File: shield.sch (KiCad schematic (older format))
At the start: 22 parts, among them J1 E5V_Conn, P1 CONN_01X03, P2 CONN_02X10, P3 CONN_01X05, P4 CONN_01X05, P5 CONN_01X05, P6 5V_CAN_SELECT, P7 CONN_02X05, Q1 Q_PMOS_DGS, U1 ST_Nucleo144_F429ZI_Morpho

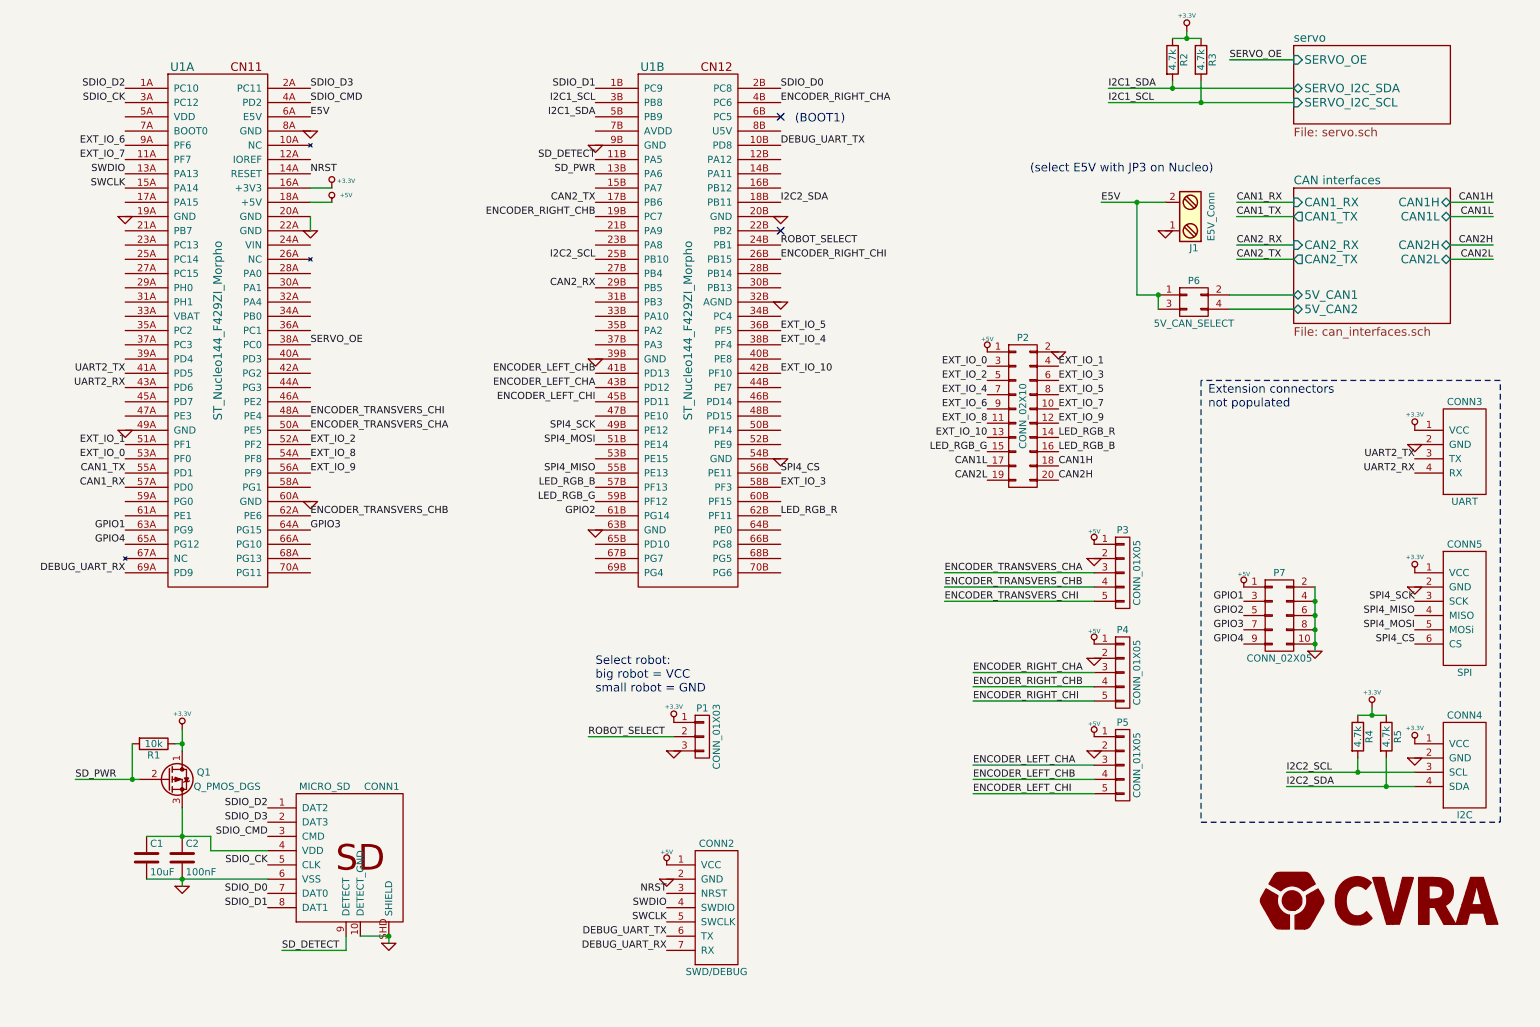
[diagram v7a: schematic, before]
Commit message: place parts in PCB
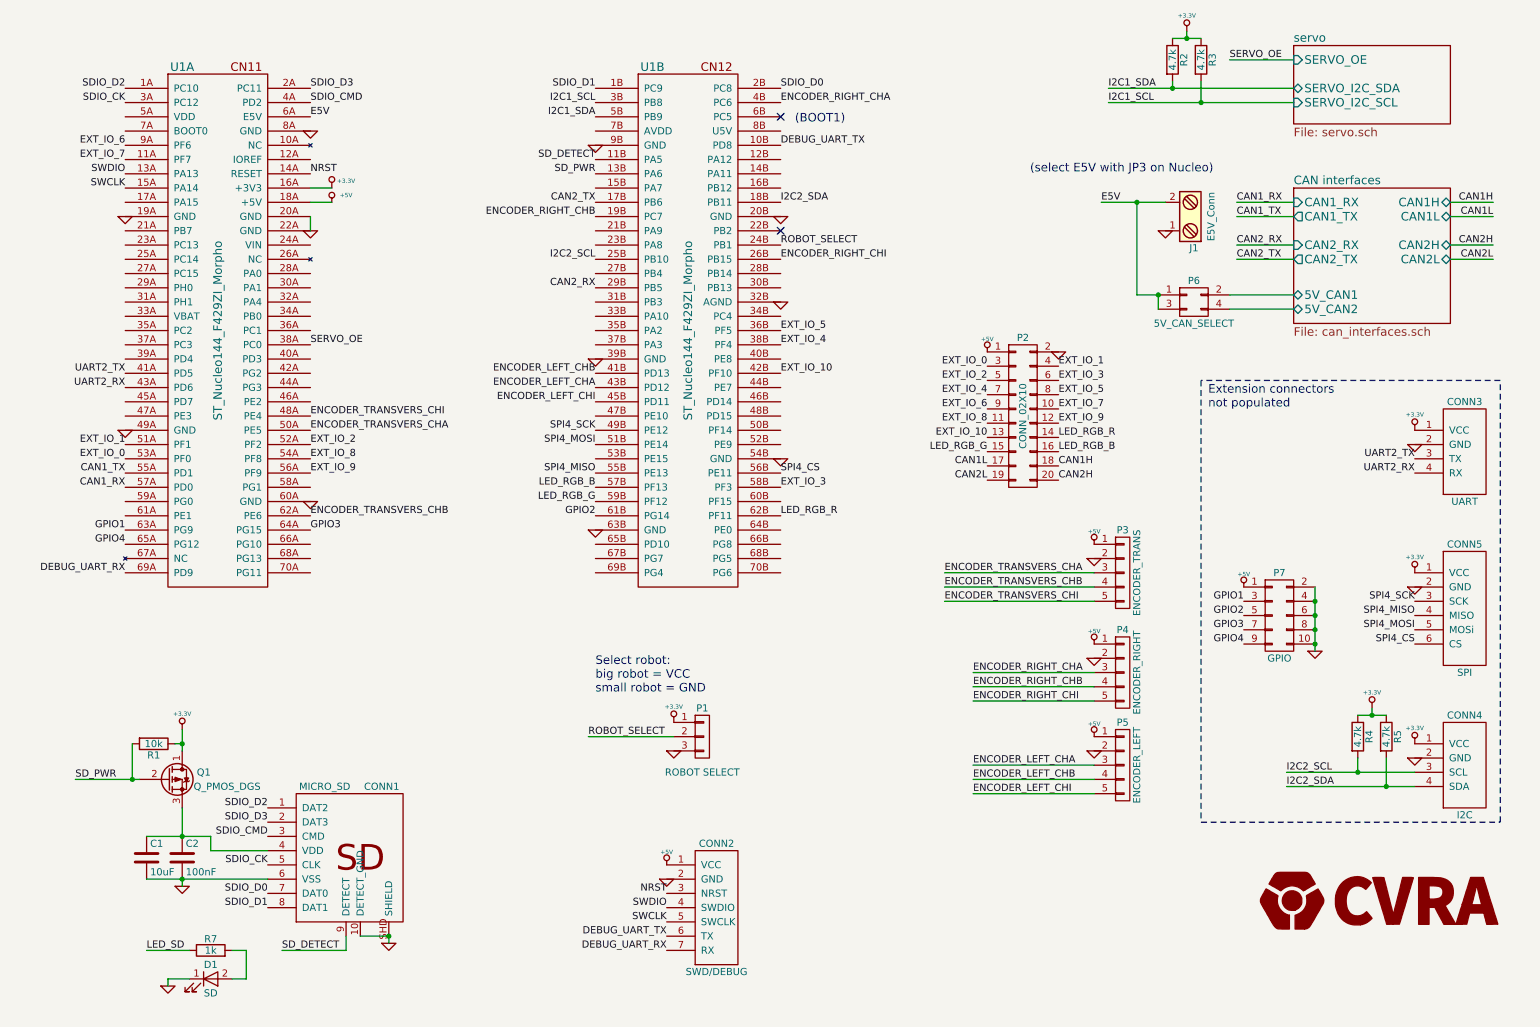
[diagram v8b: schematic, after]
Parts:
- added D1: SD, LEDs:LED_0805, symbol LED
- added R7: 1k, Resistors_SMD:R_0805, symbol R
- C2: footprint Capacitors_SMD:C_0603 -> Capacitors_SMD:C_0805
- CONN2: footprint _connectors:_Molex-PicoBlade-SMD-7 -> Connectors_Molex:Molex_PicoBlade_53047-0710_07x1.25mm_Straight
- P1: value CONN_01X03 -> ROBOT SELECT
- P2: footprint Pin_Headers:Pin_Header_Straight_2x10 -> Connect:IDC_Header_Straight_20pins
- P3: value CONN_01X05 -> ENCODER_TRANS
- P4: value CONN_01X05 -> ENCODER_RIGHT
- P5: value CONN_01X05 -> ENCODER_LEFT
- P7: value CONN_02X05 -> GPIO; footprint Pin_Headers:Pin_Header_Straight_2x05 -> Connect:IDC_Header_Straight_10pins
- R1, R2, R3, R4, R5: footprint Resistors_SMD:R_0603 -> Resistors_SMD:R_0805
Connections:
- net GND: now also D1.1 (K)
- new net: D1.2 (A), R7.2
- new net LED_SD: R7.1
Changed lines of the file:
@@
 F 0 "C2" H 1825 6650 50  0000 L CNN
 F 1 "100nF" H 1825 6450 50  0000 L CNN
-F 2 "Capacitors_SMD:C_0603" H 1838 6400 50  0001 C CNN
+F 2 "Capacitors_SMD:C_0805" H 1838 6400 50  0001 C CNN
 F 3 "" H 1800 6550 50  0000 C CNN
 	1    1800 6550
@@
 F 0 "R1" V 1680 5750 50  0000 C CNN
 F 1 "10k" V 1600 5750 50  0000 C CNN
-F 2 "Resistors_SMD:R_0603" V 1530 5750 50  0001 C CNN
+F 2 "Resistors_SMD:R_0805" V 1530 5750 50  0001 C CNN
 F 3 "" H 1600 5750 50  0000 C CNN
 	1    1600 5750
@@
 F 0 "P2" H 7700 4000 50  0000 C CNN
 F 1 "CONN_02X10" V 7700 3450 50  0000 C CNN
-F 2 "Pin_Headers:Pin_Header_Straight_2x10" H 7700 2250 50  0001 C CNN
+F 2 "Connect:IDC_Header_Straight_20pins" H 7700 2250 50  0001 C CNN
 F 3 "" H 7700 2250 50  0000 C CNN
 	1    7700 3450
@@
 P 9500 4850
 F 0 "P7" H 9500 5150 50  0000 C CNN
-F 1 "CONN_02X05" H 9500 4550 50  0000 C CNN
-F 2 "Pin_Headers:Pin_Header_Straight_2x05" H 9500 3650 50  0001 C CNN
+F 1 "GPIO" H 9500 4550 50  0000 C CNN
+F 2 "Connect:IDC_Header_Straight_10pins" H 9500 3650 50  0001 C CNN
 F 3 "" H 9500 3650 50  0000 C CNN
 	1    9500 4850
@@
 P 8400 5250
 F 0 "P4" H 8400 5550 50  0000 C CNN
-F 1 "CONN_01X05" V 8500 5250 50  0000 C CNN
+F 1 "ENCODER_RIGHT" V 8500 5250 50  0000 C CNN
 F 2 "_connectors:Molex-PicoBlade-5" H 8400 5250 50  0001 C CNN
 F 3 "" H 8400 5250 50  0000 C CNN
@@
 P 8400 5900
 F 0 "P5" H 8400 6200 50  0000 C CNN
-F 1 "CONN_01X05" V 8500 5900 50  0000 C CNN
+F 1 "ENCODER_LEFT" V 8500 5900 50  0000 C CNN
 F 2 "_connectors:Molex-PicoBlade-5" H 8400 5900 50  0001 C CNN
 F 3 "" H 8400 5900 50  0000 C CNN
@@
 P 8400 4550
 F 0 "P3" H 8400 4850 50  0000 C CNN
-F 1 "CONN_01X05" V 8500 4550 50  0000 C CNN
+F 1 "ENCODER_TRANS" V 8500 4550 50  0000 C CNN
 F 2 "_connectors:Molex-PicoBlade-5" H 8400 4550 50  0001 C CNN
 F 3 "" H 8400 4550 50  0000 C CNN
@@
 F 0 "CONN2" H 5550 7350 50  0000 C CNN
 F 1 "SWD/DEBUG" H 5550 6450 50  0000 C CNN
-F 2 "_connectors:_Molex-PicoBlade-SMD-7" H 5550 6850 50  0001 C CNN
+F 2 "Connectors_Molex:Molex_PicoBlade_53047-0710_07x1.25mm_Straight" H 5550 6850 50  0001 C CNN
 F 3 "DOCUMENTATION" H 5550 6850 50  0001 C CNN
 	1    5550 6900
@@
 P 5450 5700
 F 0 "P1" H 5450 5900 50  0000 C CNN
-F 1 "CONN_01X03" V 5550 5700 50  0000 C CNN
+F 1 "ROBOT SELECT" H 5450 5450 50  0000 C CNN
 F 2 "Pin_Headers:Pin_Header_Straight_1x03" H 5450 5700 50  0001 C CNN
 F 3 "" H 5450 5700 50  0000 C CNN
@@
 F 0 "R4" V 10130 5700 50  0000 C CNN
 F 1 "4.7k" V 10050 5700 50  0000 C CNN
-F 2 "Resistors_SMD:R_0603" V 9980 5700 50  0001 C CNN
+F 2 "Resistors_SMD:R_0805" V 9980 5700 50  0001 C CNN
 F 3 "" H 10050 5700 50  0000 C CNN
 	1    10050 5700
@@
 F 0 "R5" V 10330 5700 50  0000 C CNN
 F 1 "4.7k" V 10250 5700 50  0000 C CNN
-F 2 "Resistors_SMD:R_0603" V 10180 5700 50  0001 C CNN
+F 2 "Resistors_SMD:R_0805" V 10180 5700 50  0001 C CNN
 F 3 "" H 10250 5700 50  0000 C CNN
 	1    10250 5700
@@
 F 0 "R2" V 8830 950 50  0000 C CNN
 F 1 "4.7k" V 8750 950 50  0000 C CNN
-F 2 "Resistors_SMD:R_0603" V 8680 950 50  0001 C CNN
+F 2 "Resistors_SMD:R_0805" V 8680 950 50  0001 C CNN
 F 3 "" H 8750 950 50  0000 C CNN
 	1    8750 950
@@
 F 0 "R3" V 9030 950 50  0000 C CNN
 F 1 "4.7k" V 8950 950 50  0000 C CNN
-F 2 "Resistors_SMD:R_0603" V 8880 950 50  0001 C CNN
+F 2 "Resistors_SMD:R_0805" V 8880 950 50  0001 C CNN
 F 3 "" H 8950 950 50  0000 C CNN
 	1    8950 950
@@
 	2400 6500 2000 6500
 Wire Wire Line
-	2000 6400 2000 6500
-Wire Wire Line
-	1550 6400 2000 6400
+	2000 6500 2000 6400
+Wire Wire Line
+	2000 6400 1550 6400
 Connection ~ 1800 6400
 Wire Wire Line
@@
 Wire Wire Line
 	2700 1850 2850 1850
+$Comp
+L LED D1
+U 1 1 58BCB44B
+P 2000 7400
+F 0 "D1" H 2000 7500 50  0000 C CNN
+F 1 "SD" H 2000 7300 50  0000 C CNN
+F 2 "LEDs:LED_0805" H 2000 7400 50  0001 C CNN
+F 3 "" H 2000 7400 50  0000 C CNN
+	1    2000 7400
+	1    0    0    -1
+$EndComp
+Text Label 1550 7200 0    50   ~ 0
+LED_SD
+$Comp
+L GND #PWR040
+U 1 1 58BCD0B9
+P 1700 7450
+F 0 "#PWR040" H 1700 7450 30  0001 C CNN
+F 1 "GND" H 1700 7380 30  0001 C CNN
+F 2 "" H 1700 7450 60  0001 C CNN
+F 3 "" H 1700 7450 60  0001 C CNN
+	1    1700 7450
+	1    0    0    -1
+$EndComp
+Wire Wire Line
+	1700 7450 1700 7400
+Wire Wire Line
+	1700 7400 1850 7400
+Wire Wire Line
+	1550 7200 1850 7200
+Wire Wire Line
+	2150 7200 2250 7200
+Wire Wire Line
+	2250 7200 2250 7400
+Wire Wire Line
+	2250 7400 2150 7400
+$Comp
+L R R7
+U 1 1 58BCEE5F
+P 2000 7200
+F 0 "R7" V 2080 7200 50  0000 C CNN
+F 1 "1k" V 2000 7200 50  0000 C CNN
+F 2 "Resistors_SMD:R_0805" V 1930 7200 50  0001 C CNN
+F 3 "" H 2000 7200 50  0000 C CNN
+	1    2000 7200
+	0    -1   -1   0
+$EndComp
 $EndSCHEMATC
